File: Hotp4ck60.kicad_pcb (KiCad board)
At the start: 2 copper layers, 285 x 94.6 mm, 200 parts, among them J1 HRO_TYPE-C-31-M-12, J3 Conn_01x02_MountingPin, Q1 2N7002, SW1 RST, SW2 PWR, U1 nRF52840, U2 SRV05-4, U3 BQ24075, U4 MAX17048, Y1 32 MHz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

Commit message: Add Switch Mount pin symbol
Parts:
- removed J2: ~, Connector_PinSocket_2.54mm:PinSocket_1x04_P2.54mm_Vertical
- added TP1: TestPoint, TestPoint:TestPoint_THTPad_1.0x1.0mm_Drill0.5mm, F.Cu at (177.3, 169.1)
- added TP2: TestPoint, TestPoint:TestPoint_THTPad_D1.0mm_Drill0.5mm, F.Cu at (179.4, 169.1)
- added TP3: TestPoint, TestPoint:TestPoint_THTPad_D1.0mm_Drill0.5mm, F.Cu at (181.4, 169.1)
- added TP4: TestPoint, TestPoint:TestPoint_THTPad_D1.0mm_Drill0.5mm, F.Cu at (183.5, 169.1)
- moved SW1 2.20 mm to (186.8, 162.6), turned to 90 degrees
- turned C18 to 90 degrees
- turned C4 to 180 degrees
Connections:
- C5 pad 1: GND -> Net-(U1-XC2)
- SW2 pad MP: (no net) -> GND
- U1 pad A23: GND -> Net-(U1-XC2)
- U1 pad AC21: unconnected-(U1-P0.25-PadAC21) -> col10
- U1 pad AD22: col7 -> unconnected-(U1-TRACEDATA0/P1.00-PadAD22)
- U1 pad P23: col10 -> col5
- U1 pad R24: col13 -> col9
- U1 pad T23: col9 -> col13
- U1 pad U24: col12 -> col8
- U1 pad V23: col8 -> col12
- U1 pad W24: col11 -> col7
- U1 pad Y23: col5 -> col11
- Y1 pad 3: GND -> Net-(U1-XC2)
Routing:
- net VDDH: track 125.9 -> 106.5 mm, vias 6 -> 4
- net col13: track 274.5 -> 260.1 mm, vias 0 -> 3
- net GND: track 32.2 -> 25.9 mm, vias 344 -> 340
- net col8: track 175.4 -> 169.3 mm
- net col9: track 179.8 -> 174.8 mm
- net Net-(U1-XC2): track 0.00 -> 3.76 mm
- net col12: track 239.2 -> 235.5 mm, vias 0 -> 3
- net col11: track 220.8 -> 217.3 mm, vias 0 -> 3
- net col7: track 158.6 -> 161.0 mm
- net col10: track 196.5 -> 198.9 mm, vias 1 -> 3
- net SWDCLK: track 15.2 -> 13.0 mm
- net col5: track 116.5 -> 118.7 mm
- net SWDIO: track 11.9 -> 10.2 mm

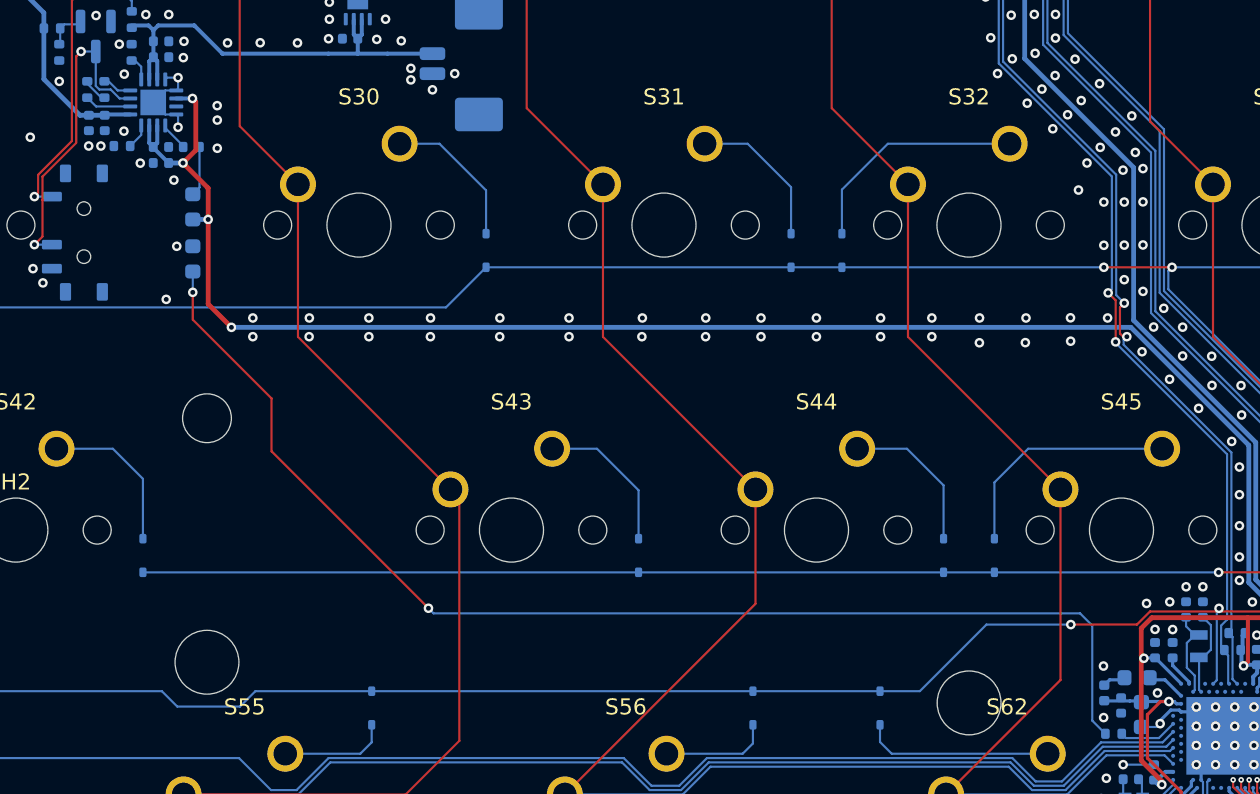
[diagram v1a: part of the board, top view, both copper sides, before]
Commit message: Update parts position
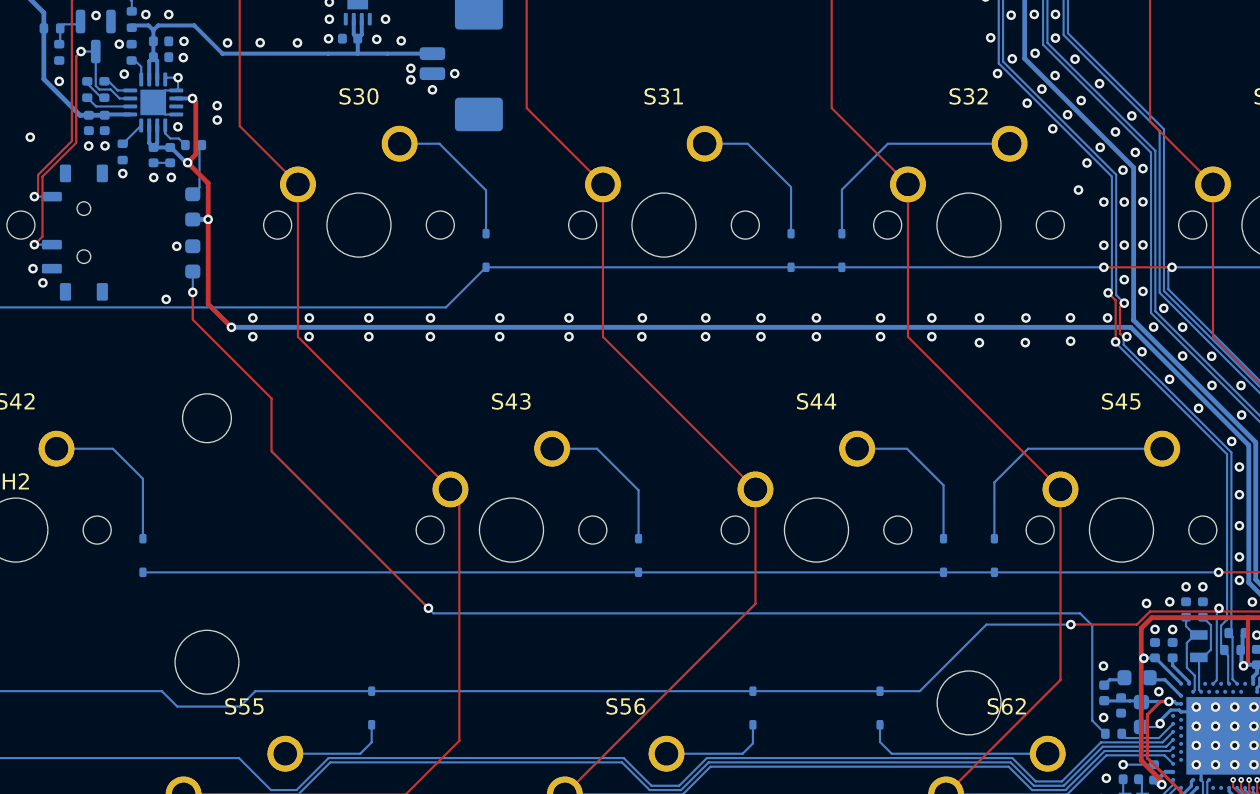
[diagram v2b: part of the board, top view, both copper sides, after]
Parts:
- moved C24 0.76 mm to (102.5, 130.6), turned to -90 degrees
- moved C23 0.69 mm to (101.5, 130.6), turned to -90 degrees
- moved R4 0.37 mm to (99.5, 130.4), turned to -90 degrees
- moved R8 0.18 mm to (104.0, 129.9)
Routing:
- net GND: track 25.9 -> 26.1 mm, vias 340 -> 339
